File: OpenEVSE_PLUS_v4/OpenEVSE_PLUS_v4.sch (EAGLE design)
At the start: 76 parts, among them IC1 MID400, IC2 MEGA8-AI, IC3 LMV358, IC4 LMV358, IC5 AQH1213, IC6 MID400, Q1 16000, Q2 2222A, Q3 2222A

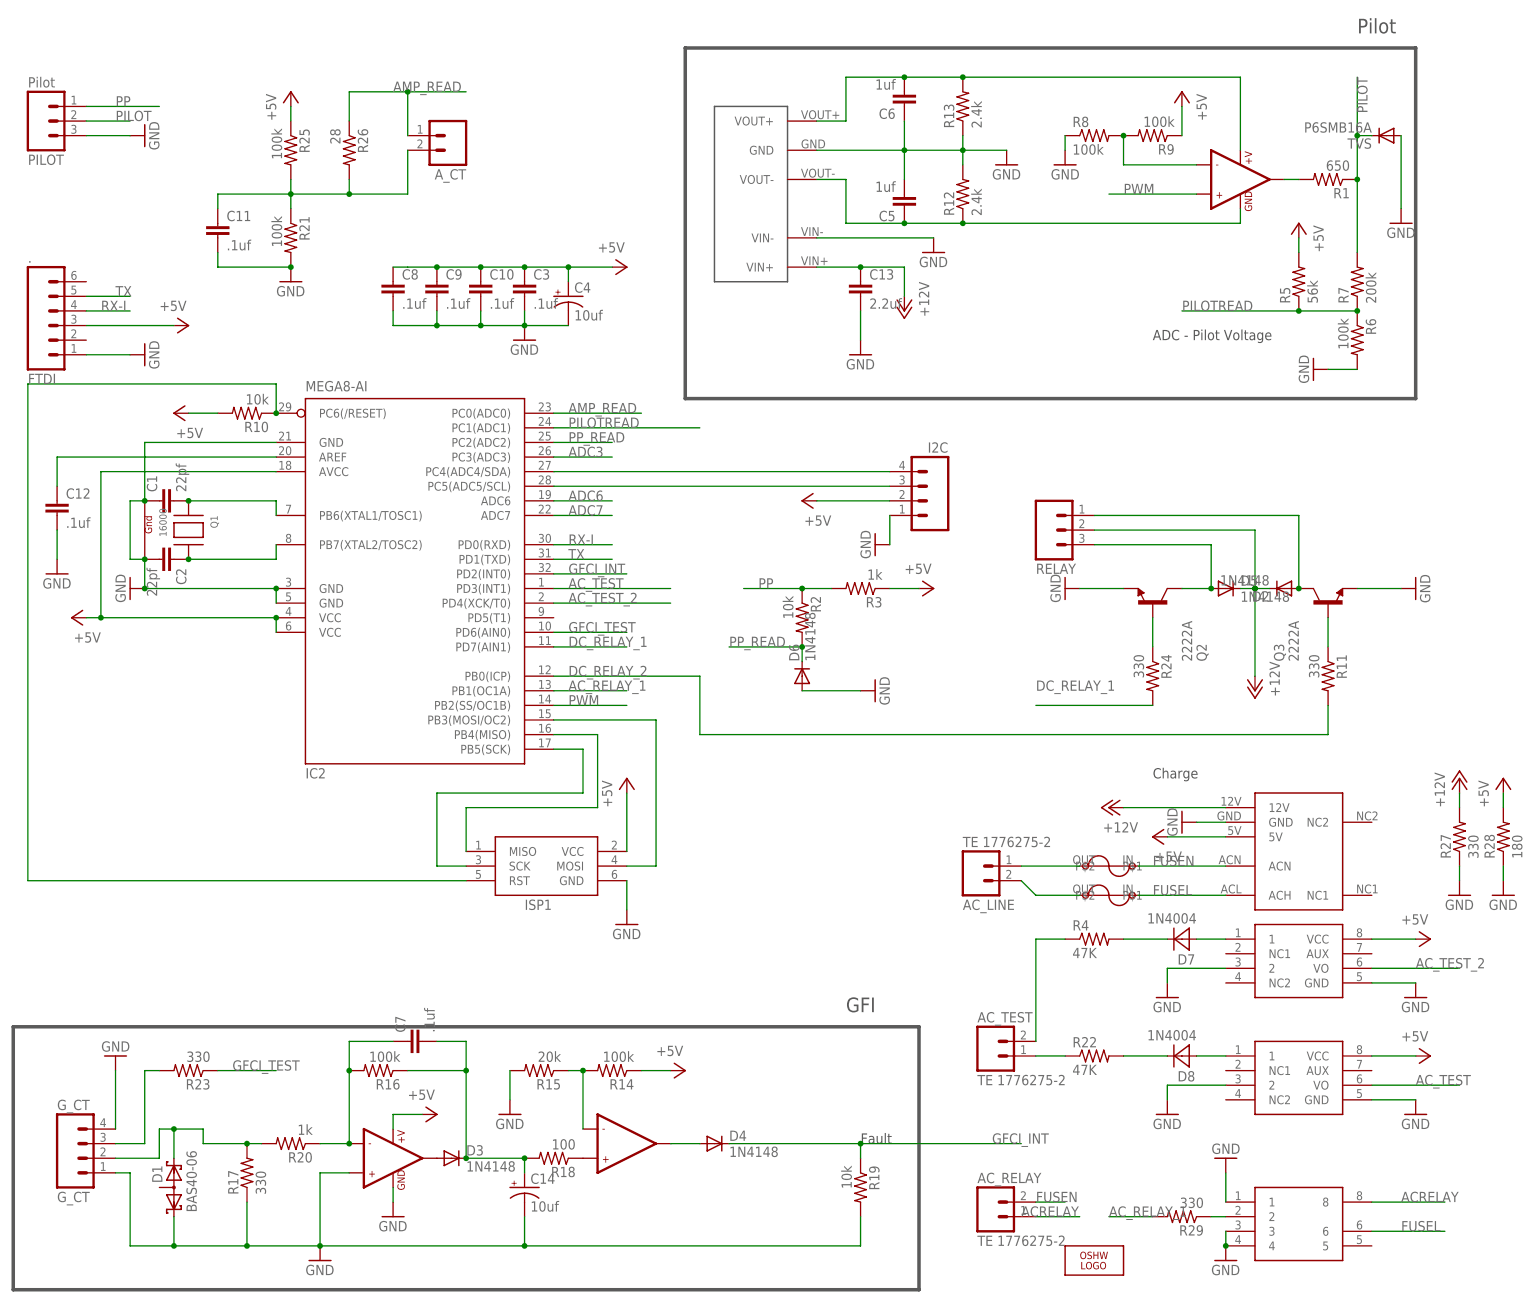
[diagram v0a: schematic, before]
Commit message: Updates to components
Updated parts values so generic footprints report the correct part when exporting Eagle generated BOM.

IC2 value 328P 
IC3 value LM358 
IC4 value LF353
TVS value P6SMB16CA
D1 value AZ23C5V6-7-F

DC/DC value MD112D-12E
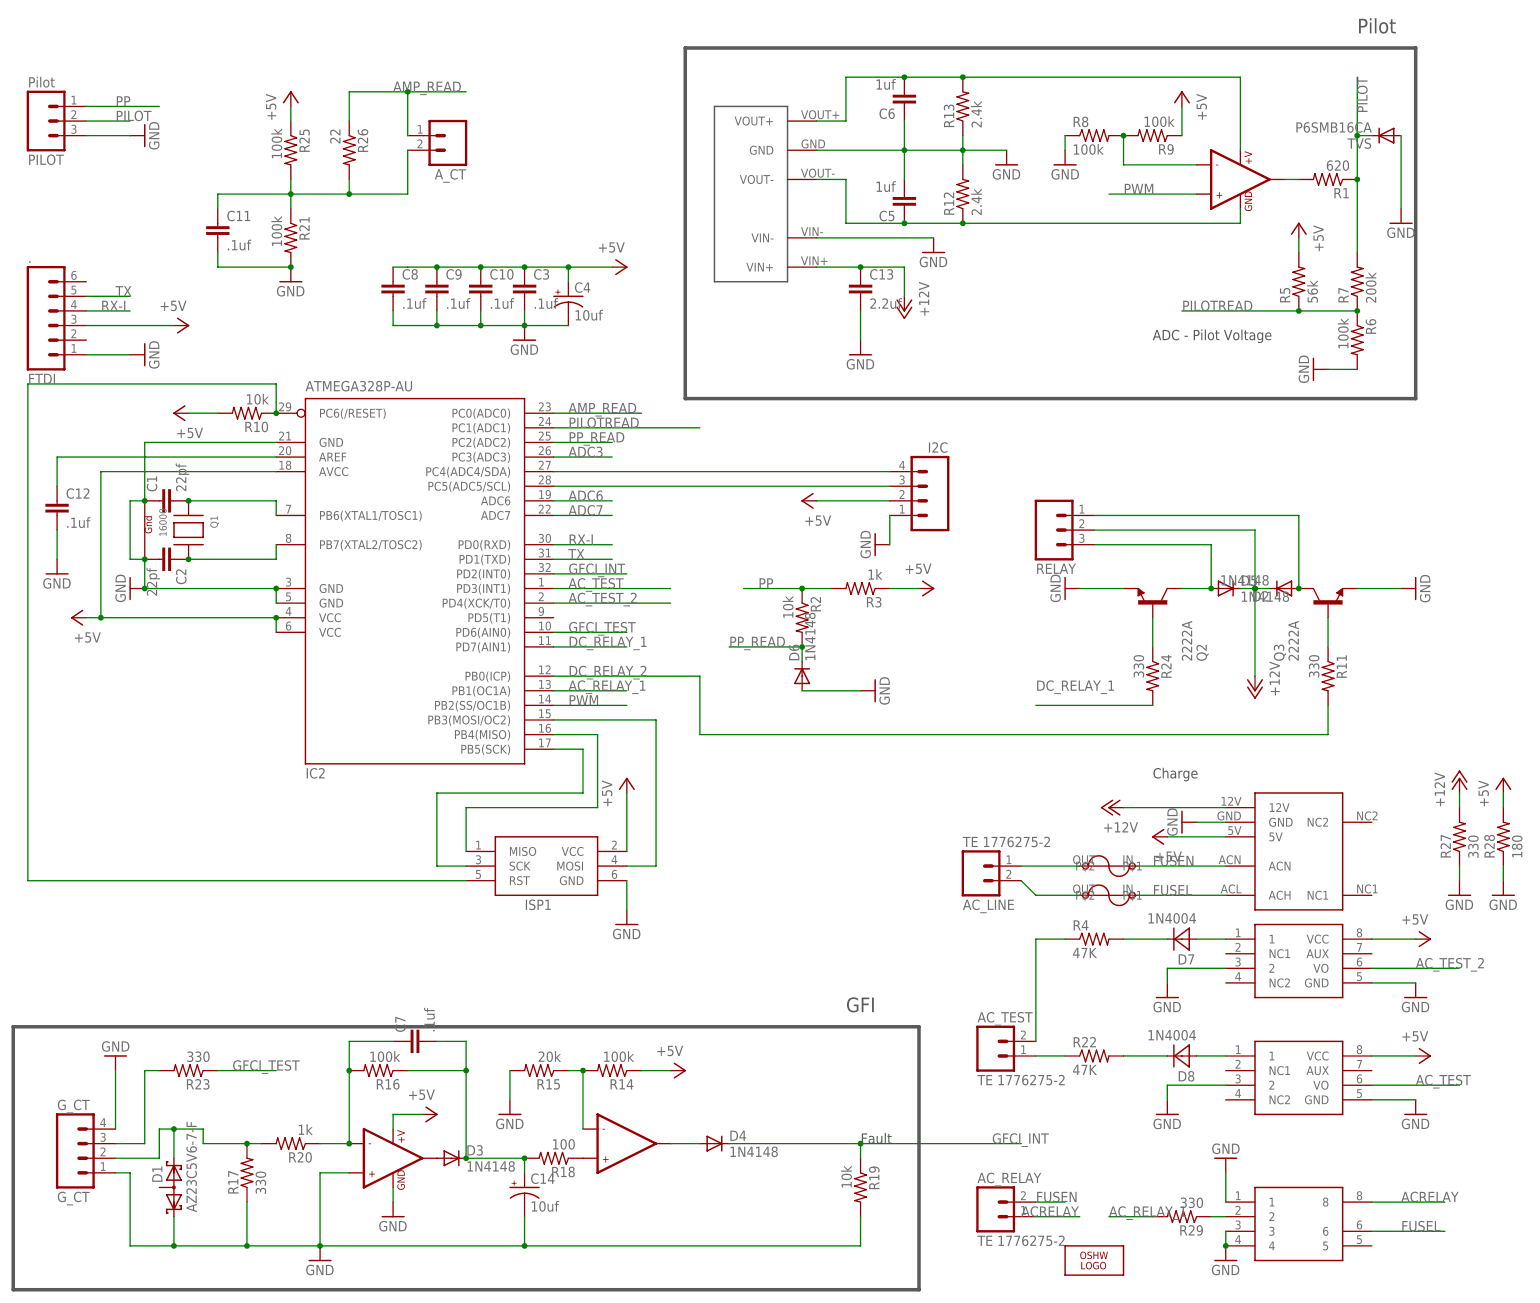
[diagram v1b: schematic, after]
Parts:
- D1: value BAS40-06 -> AZ23C5V6-7-F
- DCDC: value D107E -> MD112D-12E
- IC2: value MEGA8-AI -> ATMEGA328P-AU
- IC3: value LMV358 -> LM358
- IC4: value LMV358 -> LF353
- R1: value 650 -> 620
- R26: value 28 -> 22
- TVS: value P6SMB16A -> P6SMB16CA
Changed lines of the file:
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@@
 <?xml version="1.0" encoding="utf-8"?>
 <!DOCTYPE eagle SYSTEM "eagle.dtd">
-<eagle version="7.1.0">
+<eagle version="7.3.0">
 <drawing>
 <settings>
@@
 <part name="P+11" library="supply1" deviceset="+5V" device=""/>
 <part name="GND16" library="supply1" deviceset="GND" device=""/>
-<part name="IC2" library="atmel" deviceset="MEGA8" device="-AI"/>
-<part name="IC4" library="SparkFun" deviceset="LMV358" device=""/>
+<part name="IC2" library="atmel" deviceset="MEGA8" device="-AI" value="ATMEGA328P-AU"/>
+<part name="IC4" library="SparkFun" deviceset="LMV358" device="" value="LF353"/>
 <part name="P+13" library="supply1" deviceset="+5V" device=""/>
 <part name="GND33" library="supply1" deviceset="GND" device=""/>
@@
 <part name="R12" library="SparkFun" deviceset="RESISTOR" device="0805-RES" value="2.4k"/>
 <part name="R13" library="SparkFun" deviceset="RESISTOR" device="0805-RES" value="2.4k"/>
-<part name="R1" library="SparkFun" deviceset="RESISTOR" device="0805-RES" value="650"/>
+<part name="R1" library="SparkFun" deviceset="RESISTOR" device="0805-RES" value="620"/>
 <part name="R5" library="SparkFun" deviceset="RESISTOR" device="0805-RES" value="56k"/>
 <part name="R6" library="SparkFun" deviceset="RESISTOR" device="0805-RES" value="100k"/>
@@
 <part name="P+15" library="supply1" deviceset="+5V" device=""/>
 <part name="P+18" library="supply1" deviceset="+5V" device=""/>
-<part name="IC3" library="SparkFun" deviceset="LMV358" device=""/>
+<part name="IC3" library="SparkFun" deviceset="LMV358" device="" value="LM358"/>
 <part name="C14" library="SparkFun" deviceset="CAP_POL" device="1206" value="10uf"/>
-<part name="D1" library="diode" deviceset="BAS40-06" device=""/>
+<part name="D1" library="diode" deviceset="BAS40-06" device="" value="AZ23C5V6-7-F"/>
 <part name="C7" library="SparkFun" deviceset="CAP" device="0805" value=".1uf"/>
 <part name="R14" library="SparkFun" deviceset="RESISTOR" device="0805-RES" value="100k"/>
@@
 <part name="R20" library="SparkFun" deviceset="RESISTOR" device="0805-RES" value="1k"/>
 <part name="Q1" library="adafruit" deviceset="XTAL-4" device="-3225" value="16000"/>
-<part name="DCDC" library="Qxd" deviceset="DCDC_SIP" device="" value="D107E"/>
+<part name="DCDC" library="Qxd" deviceset="DCDC_SIP" device="" value="MD112D-12E"/>
 <part name="D2" library="diode" deviceset="DIODE-" device="SOD123" value="1N4148"/>
 <part name="D3" library="diode" deviceset="DIODE-" device="SOD123" value="1N4148"/>
 <part name="D4" library="diode" deviceset="DIODE-" device="SOD123" value="1N4148"/>
-<part name="TVS" library="diode" deviceset="DIODE-" device="SMB" value="P6SMB16A"/>
+<part name="TVS" library="diode" deviceset="DIODE-" device="SMB" value="P6SMB16CA"/>
 <part name="GND8" library="supply1" deviceset="GND" device=""/>
 <part name="Q3" library="transistor-npn" deviceset="BCX70*" device="SMD" value="2222A"/>
@@
 <part name="GND21" library="supply1" deviceset="GND" device=""/>
 <part name="P+12" library="supply1" deviceset="+5V" device=""/>
-<part name="R26" library="SparkFun" deviceset="RESISTOR" device="0805-RES" value="28"/>
+<part name="R26" library="SparkFun" deviceset="RESISTOR" device="0805-RES" value="22"/>
 <part name="A_CT" library="SparkFun" deviceset="M02" device="PTH"/>
 <part name="GND24" library="supply1" deviceset="GND" device=""/>
